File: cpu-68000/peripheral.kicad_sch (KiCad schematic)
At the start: 57 parts, among them J502 DB9_Male_MountingHoles, J503 Conn_02x03_Odd_Even, SW501 SW_DIP_x05, SW502 Blue, SW503 Black, U501 74HC2G14, U502 PCA9543A, U503 XR68C681, U504 PCF8584, U505 DS1744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

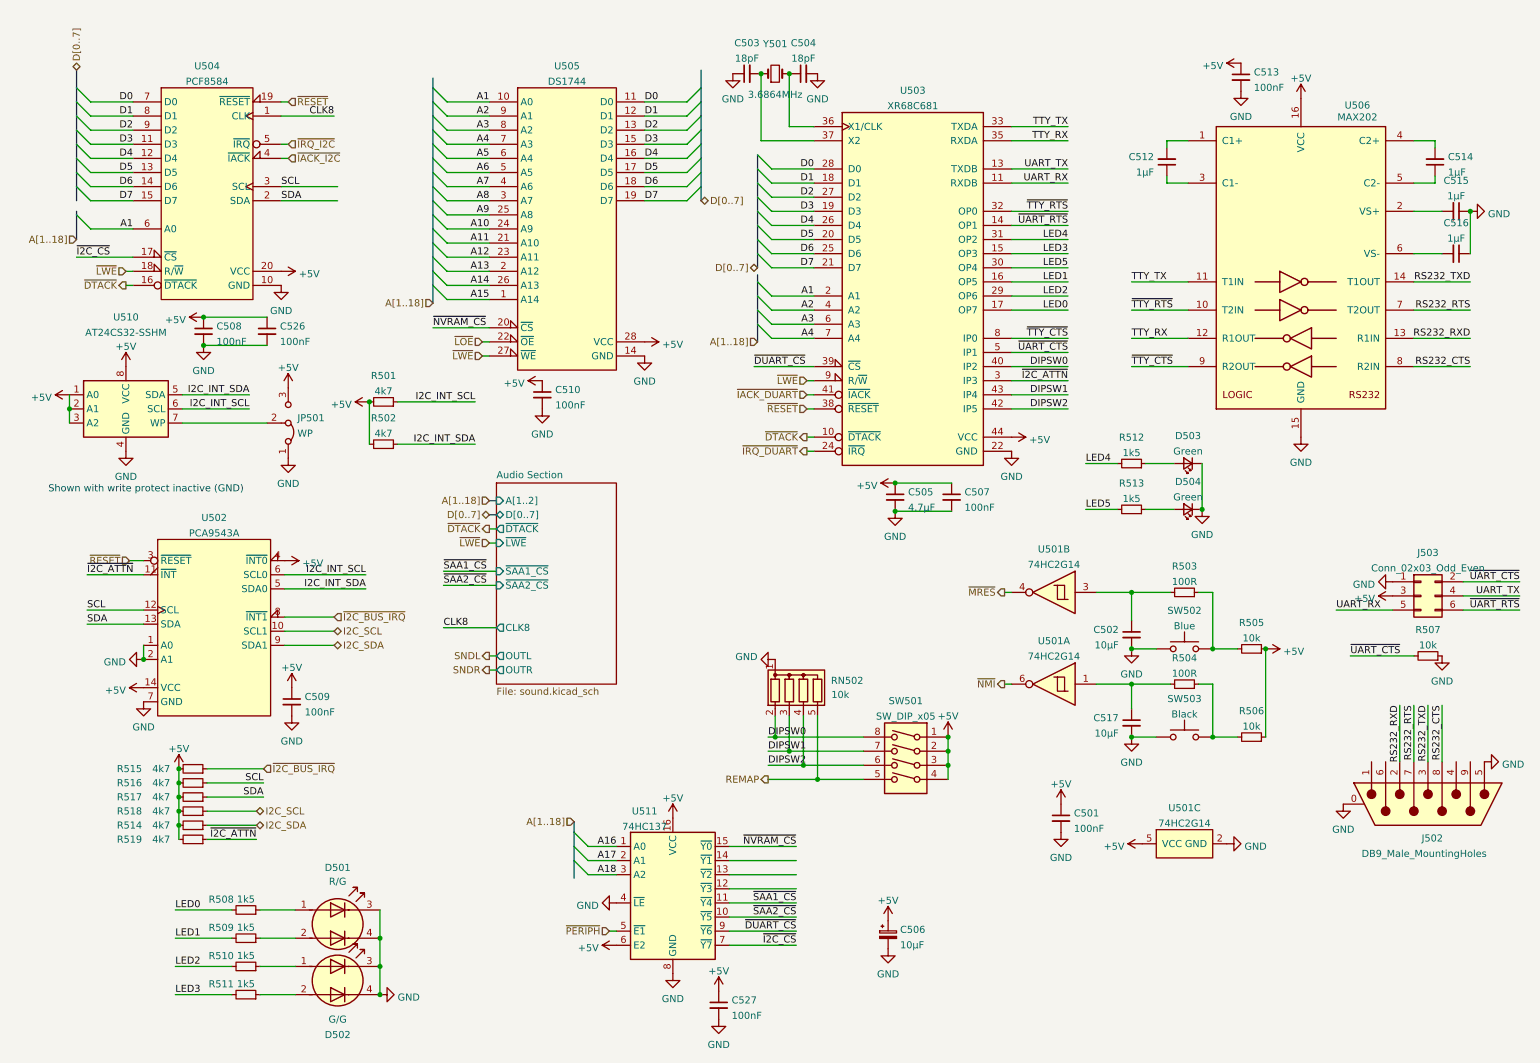
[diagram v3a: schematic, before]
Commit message: Major cleanup of CPU board
- A lot of traces got moved around to be less shitty

- Routed a few more signals to the GALs so that we can eliminate some
  discrete logic, namely for function code checking. This is critical
  since we need to reduce path length when switching the backplane bus
  buffers for each bus transaction as quick as possible.

- Actually provide a clock for the I2C master chip; it shares the clock
  with the audio chips, which is just a bit short of 8MHz.
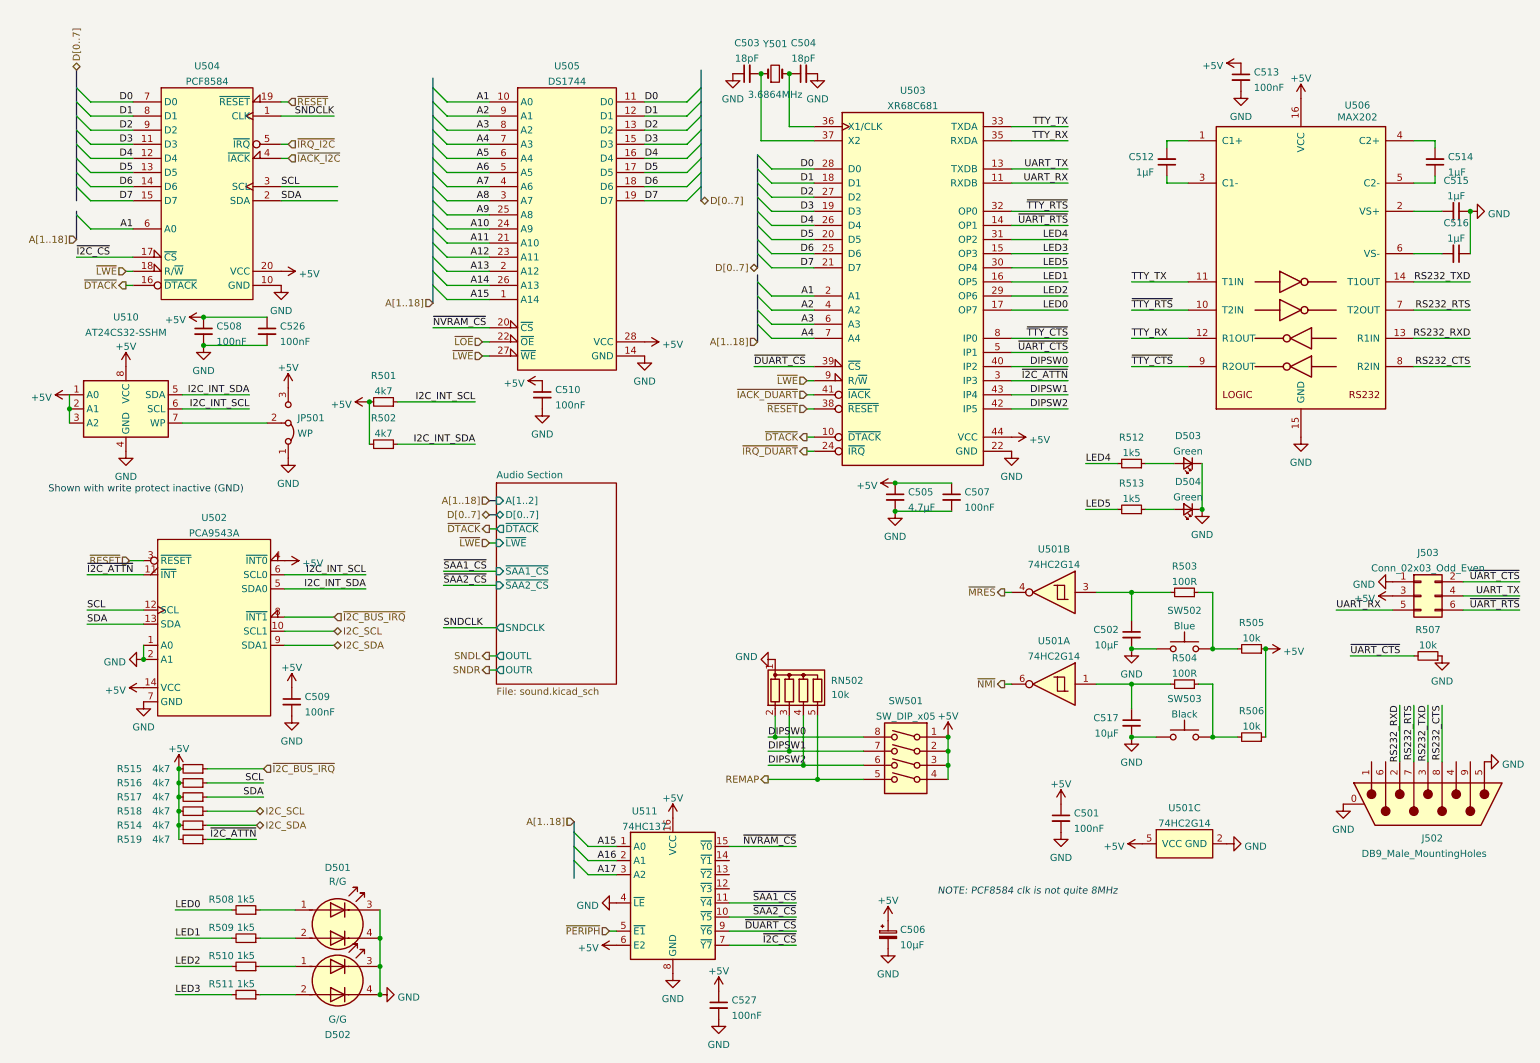
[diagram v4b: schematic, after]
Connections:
- net A18 is gone; now on net A17: U511.3 (A2)
- net A15: now also U511.1 (A0)
- net A16: now also U511.2 (A1); no longer U511.1 (A0)
- net A17: no longer U511.2 (A1)
- net CLK8 renamed SNDCLK
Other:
- sheet Audio Section ports: added SNDCLK; removed CLK8
- note added: "NOTE: PCF8584 clk is not quite 8MHz"
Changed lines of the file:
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@@
-    (stroke (width 0) (type default) (color 0 0 0 0))
-  )
-  (wire (pts (xy 140.335 162.56) (xy 152.4 162.56))
     (stroke (width 0) (type default) (color 0 0 0 0))
   )
@@
     (stroke (width 0) (type default) (color 0 0 0 0))
   )
-  (wire (pts (xy 140.335 165.1) (xy 152.4 165.1))
-    (stroke (width 0) (type default) (color 0 0 0 0))
-  )
   (wire (pts (xy 191.135 53.34) (xy 201.295 53.34))
     (stroke (width 0) (type default) (color 0 0 0 0))
@@
     (stroke (width 0) (type default) (color 0 0 0 0))
   )
-  (wire (pts (xy 140.335 167.64) (xy 152.4 167.64))
-    (stroke (width 0) (type default) (color 0 0 0 0))
-  )
   (wire (pts (xy 191.135 71.12) (xy 201.295 71.12))
     (stroke (width 0) (type default) (color 0 0 0 0))
@@
     (effects (font (size 1.27 1.27)) (justify left bottom))
   )
+  (text "NOTE: PCF8584 clk is not quite 8MHz" (at 177.8 168.91 0)
+    (effects (font (size 1.27 1.27) italic) (justify left bottom))
+  )
   (label "I2C_INT_SCL" (at 74.93 111.125 180)
     (effects (font (size 1.27 1.27)) (justify right bottom))
@@
     (effects (font (size 1.27 1.27)) (justify right bottom))
   )
-  (label "A17" (at 120.015 162.56 180)
+  (label "A16" (at 120.015 162.56 180)
     (effects (font (size 1.27 1.27)) (justify right bottom))
   )
@@
     (effects (font (size 1.27 1.27)) (justify right bottom))
   )
-  (label "A18" (at 120.015 165.1 180)
+  (label "A17" (at 120.015 165.1 180)
     (effects (font (size 1.27 1.27)) (justify right bottom))
   )
@@
     (effects (font (size 1.27 1.27)) (justify right bottom))
   )
-  (label "A16" (at 120.015 160.02 180)
+  (label "A15" (at 120.015 160.02 180)
     (effects (font (size 1.27 1.27)) (justify right bottom))
   )
@@
     (effects (font (size 1.27 1.27)) (justify right bottom))
   )
-  (label "CLK8" (at 88.9 120.65 0)
+  (label "SNDCLK" (at 88.9 120.65 0)
     (effects (font (size 1.27 1.27)) (justify left bottom))
   )
@@
     (effects (font (size 1.27 1.27)) (justify right bottom))
   )
-  (label "CLK8" (at 69.215 28.575 180)
+  (label "SNDCLK" (at 69.215 28.575 180)
     (effects (font (size 1.27 1.27)) (justify right bottom))
   )
@@
       (effects (font (size 1.27 1.27)) (justify left))
     )
-    (pin "CLK8" output (at 98.425 120.65 180)
-      (effects (font (size 1.27 1.27)) (justify left))
-    )
+    (pin "SNDCLK" output (at 98.425 120.65 180)
+      (effects (font (size 1.27 1.27)) (justify left))
+    )

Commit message: Schematic cleanup and ERC fixes
- Fixed many errors about duplicate or unassigned pins, and fixed some
  of the symbols and their pins directions.

- More minor tweaks to the pcb.
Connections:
- no-connect marks 0 -> 7
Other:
- note removed: "NOTE: PCF8584 clk is not quite 8MHz"
- company: (none) -> Tristan Seifert
- title: (none) -> 68komputer CPU Board
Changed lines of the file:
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@@
 (kicad_sch (version 20211123) (generator eeschema)
   (paper "A4")
+  (title_block
+    (title "68komputer CPU Board")
+    (date "2021-12-11")
+    (rev "1")
+    (company "Tristan Seifert")
+    (comment 1 "PCF8584 clk is not quite 8MHz; I²C clocks will be incorrect")
+  )
   (junction (at 41.275 148.59) (diameter 0) (color 0 0 0 0)
   )
@@
   (junction (at 227.33 124.46) (diameter 0) (color 0 0 0 0)
   )
+  (no_connect (at 255.905 144.78))
+  (no_connect (at 258.445 144.78))
+  (no_connect (at 273.685 144.78))
+  (no_connect (at 271.145 144.78))
+  (no_connect (at 140.335 167.64))
+  (no_connect (at 140.335 165.1))
+  (no_connect (at 140.335 162.56))
   (bus_entry (at 132.715 41.275) (size 2.54 -2.54)
     (stroke (width 0) (type default) (color 0 0 0 0))
@@
   (text "Shown with write protect inactive (GND)" (at 17.78 96.52 0)
     (effects (font (size 1.27 1.27)) (justify left bottom))
-  )
-  (text "NOTE: PCF8584 clk is not quite 8MHz" (at 177.8 168.91 0)
-    (effects (font (size 1.27 1.27) italic) (justify left bottom))
   )
   (label "I2C_INT_SCL" (at 74.93 111.125 180)
@@
       (effects (font (size 1.27 1.27)) hide)
     )
+    (pin "1")
     (pin "10")
     (pin "11")
+    (pin "12")
     (pin "13")
     (pin "14")
@@
     (pin "21")
     (pin "22")
+    (pin "23")
     (pin "24")
     (pin "25")
@@
     (pin "32")
     (pin "33")
+    (pin "34")
     (pin "35")
     (pin "36")

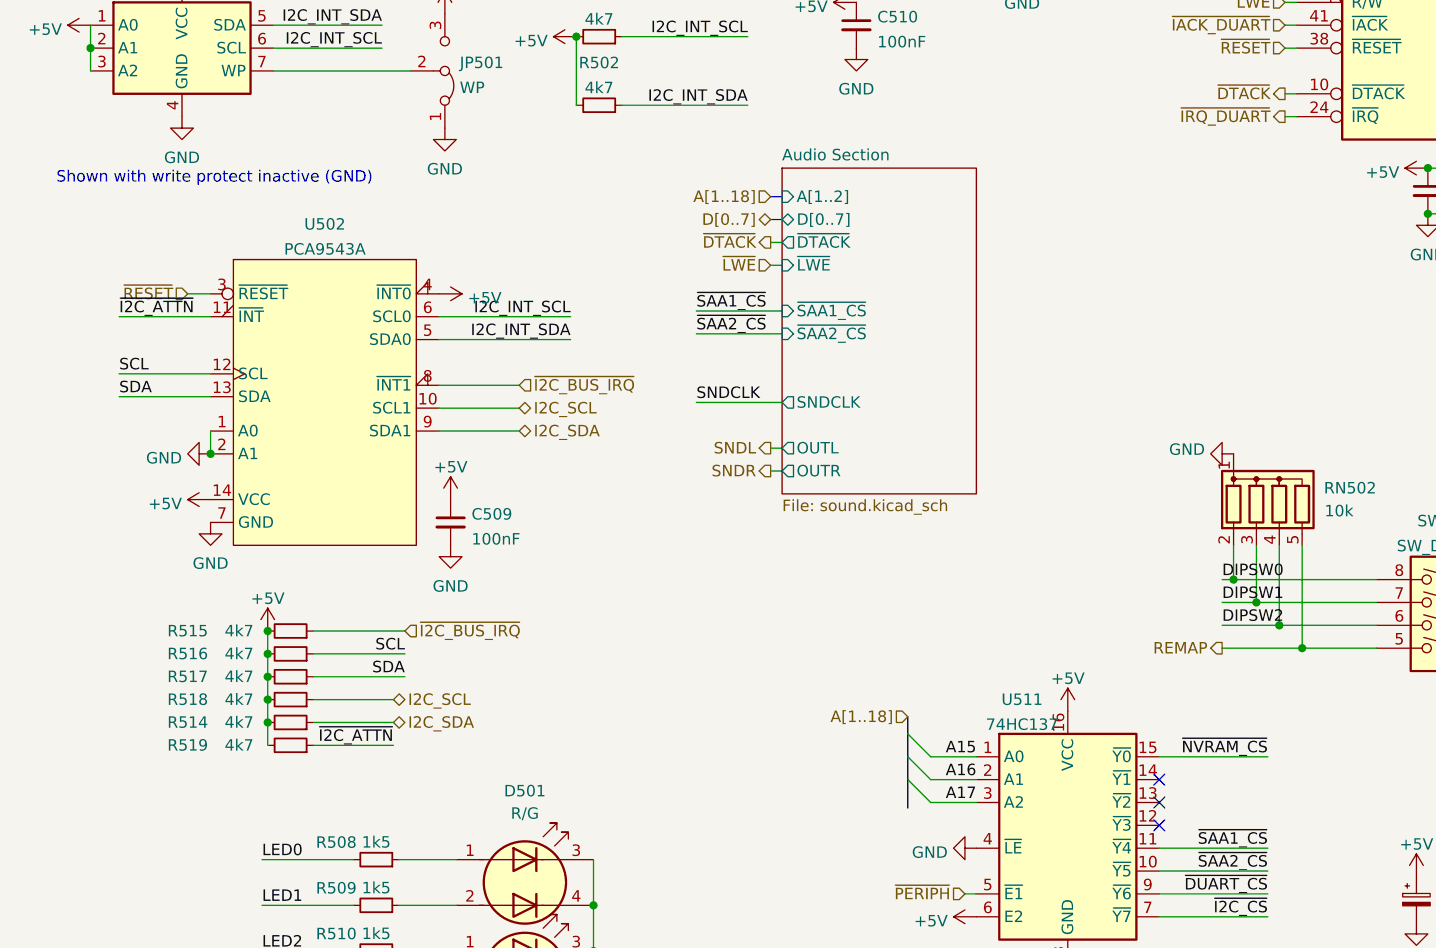
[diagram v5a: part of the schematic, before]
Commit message: More minor tweaks to CPU board
- Added an I2C expansion header, which some GPIO stuff could be
  connected to for testing, and to probe the on-board I2C bus with an
  external logic analyzer.

- The parts on it are frozen at this point since they have been ordered
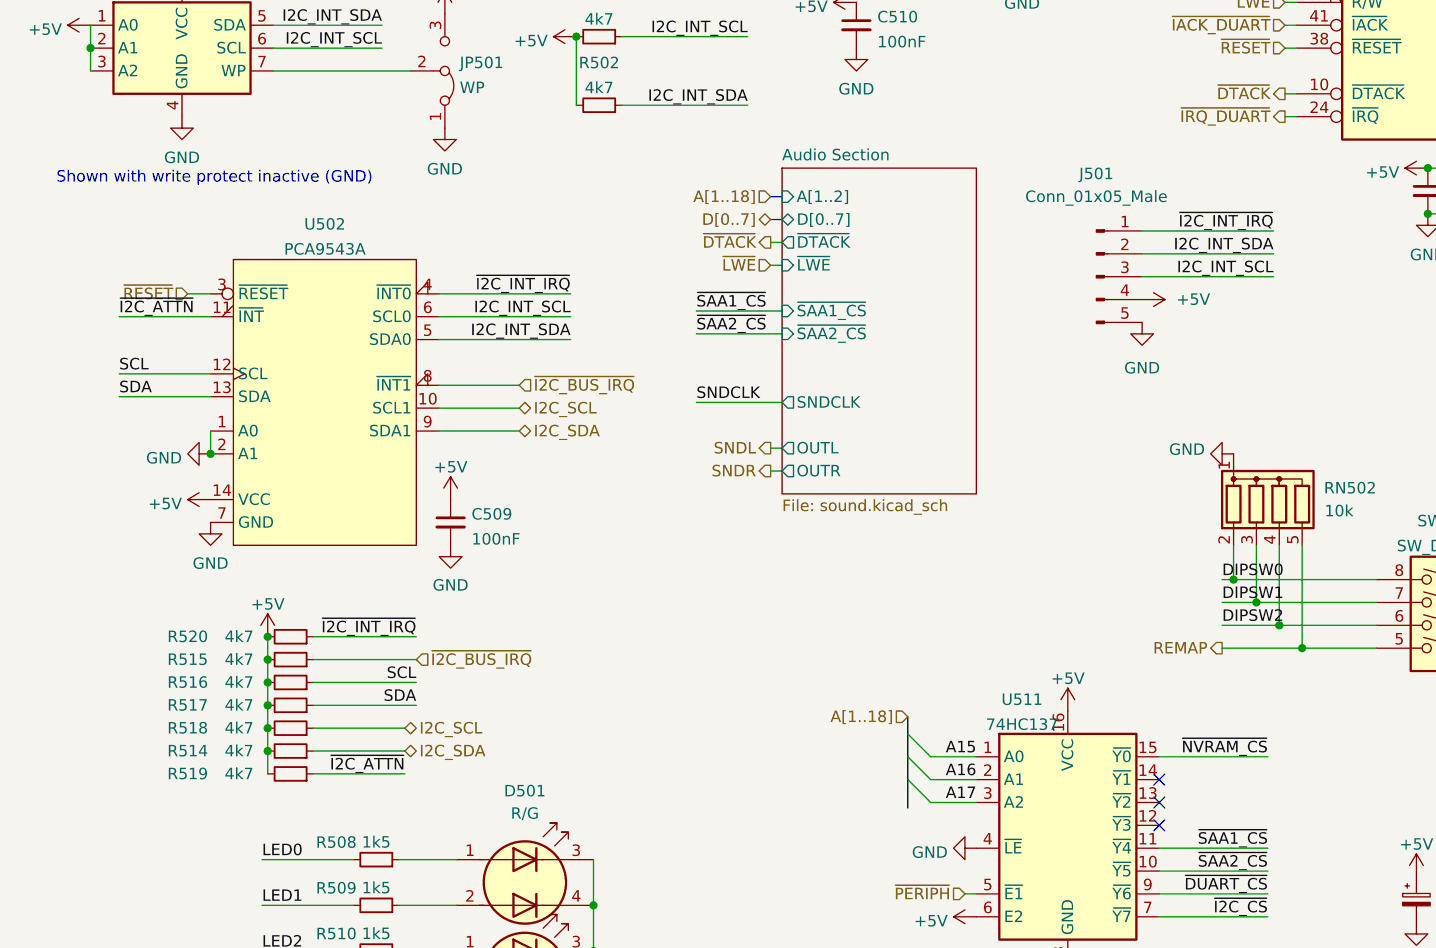
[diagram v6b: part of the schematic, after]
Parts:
- added J501: Conn_01x05_Male, Connector_PinHeader_2.54mm:PinHeader_1x05_P2.54mm_Vertical, symbol Connector:Conn_01x05_Male
- added R520: 4k7, Resistor_SMD:R_0805_2012Metric, symbol Device:R_Small
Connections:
- net +5V: now also J501.4 (Pin_4), R520.2; no longer U502.4 (~{INT0})
- net GND: now also J501.5 (Pin_5)
- net I2C_INT_SCL: now also J501.3 (Pin_3)
- net I2C_INT_SDA: now also J501.2 (Pin_2)
- new net ~{I2C_INT_IRQ}: J501.1 (Pin_1), R520.1, U502.4 (~{INT0})
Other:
- moved on the sheet: R514, R515, R516, R517, R518, R519
